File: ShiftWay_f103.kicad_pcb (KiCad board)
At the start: 2 copper layers, 120 parts, among them J1 GPIO, J2 3v3/GND, Q1 MMBTA42, Q2 MMBT5551L, Q3 STN93003, U1 STM32F103C8Tx, U2 XL7005A, U3 ICW6215, U4 LM1117DT-3.3, U5 MPU-6500

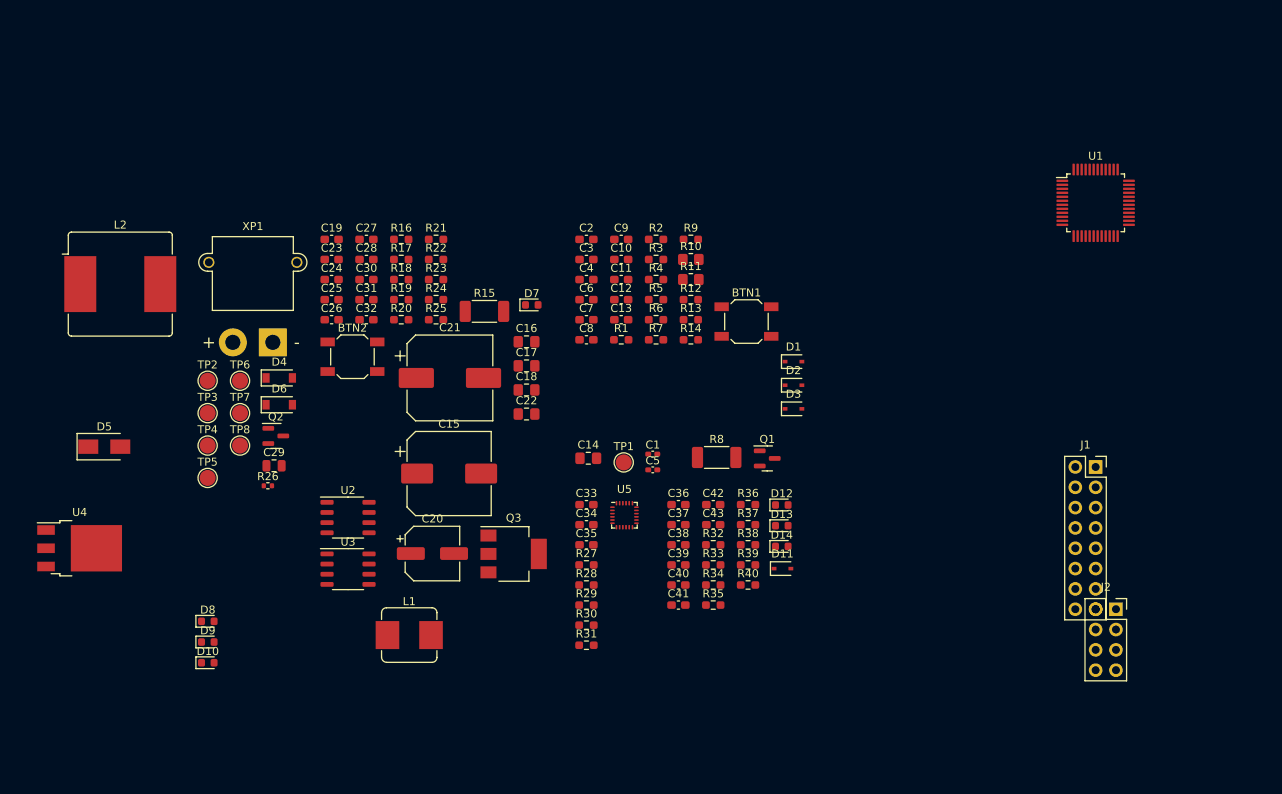
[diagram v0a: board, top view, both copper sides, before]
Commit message: Fixed short cirquit, minors
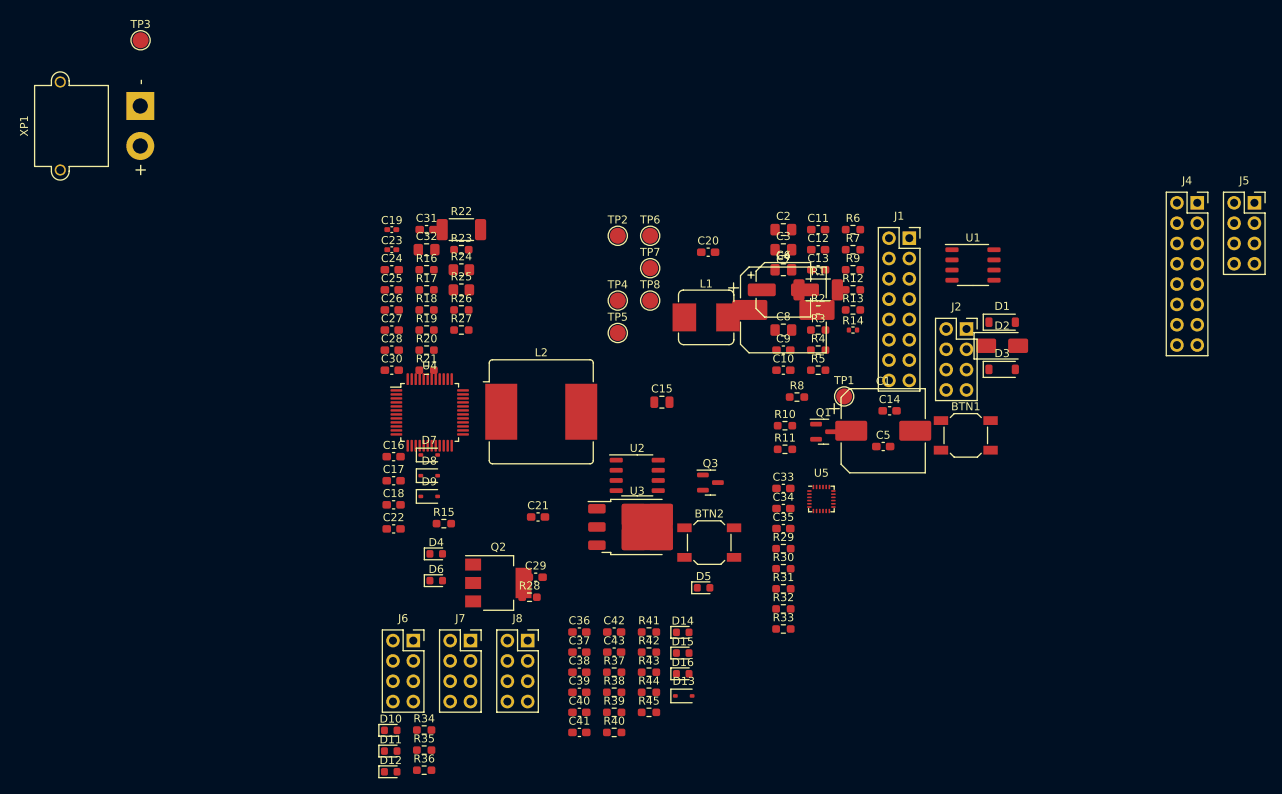
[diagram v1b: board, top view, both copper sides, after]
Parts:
- added D15: LED_G, LED_SMD:LED_0603_1608Metric, F.Cu at (118.6, 109.6)
- added D16: LED_G, LED_SMD:LED_0603_1608Metric, F.Cu at (118.6, 112.2)
- added J4: GPIO, Connector_PinSocket_2.54mm:PinSocket_2x08_P2.54mm_Vertical, F.Cu at (182.9, 53.3)
- added J5: GND/3V3, Connector_PinSocket_2.54mm:PinSocket_2x04_P2.54mm_Vertical, F.Cu at (190.0, 53.3)
- added J6: Conn_02x04, Connector_PinSocket_2.54mm:PinSocket_2x04_P2.54mm_Vertical, F.Cu at (84.9, 108.1)
- added J7: Conn_02x04, Connector_PinSocket_2.54mm:PinSocket_2x04_P2.54mm_Vertical, F.Cu at (92.0, 108.1)
- added J8: Conn_02x04, Connector_PinSocket_2.54mm:PinSocket_2x04_P2.54mm_Vertical, F.Cu at (99.2, 108.1)
- added R41: 4k3, Resistor_SMD:R_0603_1608Metric_Pad0.98x0.95mm_HandSolder, F.Cu at (114.3, 107.0)
- added R42: 4k3, Resistor_SMD:R_0603_1608Metric_Pad0.98x0.95mm_HandSolder, F.Cu at (114.3, 109.5)
- added R43: 680R, Resistor_SMD:R_0603_1608Metric_Pad0.98x0.95mm_HandSolder, F.Cu at (114.3, 112.0)
- added R44: 680R, Resistor_SMD:R_0603_1608Metric_Pad0.98x0.95mm_HandSolder, F.Cu at (114.3, 114.5)
- added R45: 680R, Resistor_SMD:R_0603_1608Metric_Pad0.98x0.95mm_HandSolder, F.Cu at (114.3, 117.0)
- C1: value 18pF -> 22uF 200v; footprint Capacitor_SMD:C_0402_1005Metric_Pad0.74x0.62mm_HandSolder -> Capacitor_SMD:CP_Elec_10x10
- C11, C39, C41: value 0.1uF -> 10uF
- C14, C16, C17, C22: footprint Capacitor_SMD:C_0805_2012Metric_Pad1.18x1.45mm_HandSolder -> Capacitor_SMD:C_0603_1608Metric_Pad1.08x0.95mm_HandSolder
- C15: value 22uF 200v -> 10uF; footprint Capacitor_SMD:CP_Elec_10x10 -> Capacitor_SMD:C_0805_2012Metric
- C18: value 2.2uF 50v -> 10uF; footprint Capacitor_SMD:C_0805_2012Metric_Pad1.18x1.45mm_HandSolder -> Capacitor_SMD:C_0603_1608Metric_Pad1.08x0.95mm_HandSolder
- C19: value 22nF -> 18pF; footprint Capacitor_SMD:C_0603_1608Metric_Pad1.08x0.95mm_HandSolder -> Capacitor_SMD:C_0402_1005Metric_Pad0.74x0.62mm_HandSolder
- C2, C3, C8: footprint Capacitor_SMD:C_0603_1608Metric_Pad1.08x0.95mm_HandSolder -> Capacitor_SMD:C_0805_2012Metric_Pad1.18x1.45mm_HandSolder
- C20: value 220uF 16v -> 0.1uF; footprint Capacitor_SMD:CP_Elec_6.3x7.7 -> Capacitor_SMD:C_0603_1608Metric_Pad1.08x0.95mm_HandSolder
- C21: value 470uF 25v -> 0.1uF; footprint Capacitor_SMD:CP_Elec_10x10.5 -> Capacitor_SMD:C_0603_1608Metric_Pad1.08x0.95mm_HandSolder
- C23: value 0.1uF -> 18pF; footprint Capacitor_SMD:C_0603_1608Metric_Pad1.08x0.95mm_HandSolder -> Capacitor_SMD:C_0402_1005Metric_Pad0.74x0.62mm_HandSolder
- C25, C40, C42: value 10uF -> 0.1uF
- C29: value 10uF -> 0.1uF; footprint Capacitor_SMD:C_0805_2012Metric -> Capacitor_SMD:C_0603_1608Metric_Pad1.08x0.95mm_HandSolder
- C32: value 10uF -> 0.1uF; footprint Capacitor_SMD:C_0603_1608Metric_Pad1.08x0.95mm_HandSolder -> Capacitor_SMD:C_0805_2012Metric_Pad1.18x1.45mm_HandSolder
- C4: value 0.1uF -> 2.2uF 50v; footprint Capacitor_SMD:C_0603_1608Metric_Pad1.08x0.95mm_HandSolder -> Capacitor_SMD:C_0805_2012Metric_Pad1.18x1.45mm_HandSolder
- C5: value 18pF -> 22nF; footprint Capacitor_SMD:C_0402_1005Metric_Pad0.74x0.62mm_HandSolder -> Capacitor_SMD:C_0603_1608Metric_Pad1.08x0.95mm_HandSolder
- C6: value 0.1uF -> 220uF 16v; footprint Capacitor_SMD:C_0603_1608Metric_Pad1.08x0.95mm_HandSolder -> Capacitor_SMD:CP_Elec_6.3x7.7
- C7: value 0.1uF -> 470uF 25v; footprint Capacitor_SMD:C_0603_1608Metric_Pad1.08x0.95mm_HandSolder -> Capacitor_SMD:CP_Elec_10x10.5
- D1, D3: value 1N4148WS -> MBR0530; footprint Diode_SMD:D_SOD-323 -> Diode_SMD:D_SOD-123
- D11: value 1N4148WS -> LED_R; footprint Diode_SMD:D_SOD-323 -> LED_SMD:LED_0603_1608Metric
- D12: value LED_G -> LED_R
- D13, D7: value LED_G -> 1N4148WS; footprint LED_SMD:LED_0603_1608Metric -> Diode_SMD:D_SOD-323
- D2: value 1N4148WS -> US1D; footprint Diode_SMD:D_SOD-323 -> Diode_SMD:D_SMA
- D4, D6: value MBR0530 -> LED_G; footprint Diode_SMD:D_SOD-123 -> LED_SMD:LED_0603_1608Metric
- D5: value US1D -> LED_G; footprint Diode_SMD:D_SMA -> LED_SMD:LED_0603_1608Metric
- D8, D9: value LED_R -> 1N4148WS; footprint LED_SMD:LED_0603_1608Metric -> Diode_SMD:D_SOD-323
- Q1: value MMBTA42 -> MMBT5551L
- Q2: value MMBT5551L -> STN93003; footprint Package_TO_SOT_SMD:SOT-23 -> Package_TO_SOT_SMD:SOT-223-3_TabPin2
- Q3: value STN93003 -> MMBTA42; footprint Package_TO_SOT_SMD:SOT-223-3_TabPin2 -> Package_TO_SOT_SMD:SOT-23
- R1: value 4k3 -> 100R 1W; footprint Resistor_SMD:R_0603_1608Metric_Pad0.98x0.95mm_HandSolder -> Resistor_SMD:R_2010_5025Metric_Pad1.40x2.65mm_HandSolder
- R10: value 81k 1% -> 2k2; footprint Resistor_SMD:R_0805_2012Metric_Pad1.20x1.40mm_HandSolder -> Resistor_SMD:R_0603_1608Metric_Pad0.98x0.95mm_HandSolder
- R11: value 2k2 1% -> 2k2; footprint Resistor_SMD:R_0805_2012Metric_Pad1.20x1.40mm_HandSolder -> Resistor_SMD:R_0603_1608Metric_Pad0.98x0.95mm_HandSolder
- R12: value 2k2 -> 1k
- R14: value 2k2 -> 680R; footprint Resistor_SMD:R_0603_1608Metric_Pad0.98x0.95mm_HandSolder -> Resistor_SMD:R_0402_1005Metric
- R15: value 100R 1W -> 4k3; footprint Resistor_SMD:R_2010_5025Metric_Pad1.40x2.65mm_HandSolder -> Resistor_SMD:R_0603_1608Metric_Pad0.98x0.95mm_HandSolder
- R19: value 6k8 -> 2k2
- R21, R23: value 81k -> 2k2
- R22: value 6k8 -> 1k 1W; footprint Resistor_SMD:R_0603_1608Metric_Pad0.98x0.95mm_HandSolder -> Resistor_SMD:R_2010_5025Metric_Pad1.40x2.65mm_HandSolder
- R24: value 2k2 -> 81k 1%; footprint Resistor_SMD:R_0603_1608Metric_Pad0.98x0.95mm_HandSolder -> Resistor_SMD:R_0805_2012Metric_Pad1.20x1.40mm_HandSolder
- R25: value 2k2 -> 2k2 1%; footprint Resistor_SMD:R_0603_1608Metric_Pad0.98x0.95mm_HandSolder -> Resistor_SMD:R_0805_2012Metric_Pad1.20x1.40mm_HandSolder
- R26: footprint Resistor_SMD:R_0402_1005Metric -> Resistor_SMD:R_0603_1608Metric_Pad0.98x0.95mm_HandSolder
- R27, R28: value 10k -> 2k2
- R32, R33: value 4k3 -> 10k
- R34, R35, R36: value 4k3 -> 1k
- R38, R39, R40: value 2k2 -> 4k3
- R5: value 2k2 -> 6k8
- R7, R9: value 2k2 -> 81k
- R8: value 1k 1W -> 6k8; footprint Resistor_SMD:R_2010_5025Metric_Pad1.40x2.65mm_HandSolder -> Resistor_SMD:R_0603_1608Metric_Pad0.98x0.95mm_HandSolder
- TP1: value SENBAT -> PWRON
- TP2: value PWRON -> PWRBUT
- TP3: value PWRBUT -> VBAT1
- TP4: value VBAT1 -> VBAT2
- TP5: value VBAT2 -> 5V
- TP6: value 5V -> 12V
- TP7: value 12V -> 3V3
- TP8: value 3V3 -> SENBAT
- U1: value STM32F103C8Tx -> XL7005A; footprint Package_QFP:LQFP-48_7x7mm_P0.5mm -> Package_SO:SOP-8_3.9x4.9mm_P1.27mm
- U2: value XL7005A -> ICW6215
- U3: value ICW6215 -> LM1117DT-3.3; footprint Package_SO:SOP-8_3.9x4.9mm_P1.27mm -> Package_TO_SOT_SMD:TO-252-3_TabPin2
- U4: value LM1117DT-3.3 -> STM32F103C8Tx; footprint Package_TO_SOT_SMD:TO-252-3_TabPin2 -> Package_QFP:LQFP-48_7x7mm_P0.5mm
- moved D5 77.0 mm to (121.2, 101.5)
- moved D12 59.2 mm to (82.1, 124.5)
- moved L2 55.0 mm to (100.9, 79.5)
- moved TP2 54.4 mm to (110.4, 57.5)
- moved TP4 54.4 mm to (110.4, 65.6)
- moved TP5 54.4 mm to (110.4, 69.6)
- moved TP6 54.4 mm to (114.5, 57.5)
- moved TP7 54.4 mm to (114.5, 61.5)
- moved TP8 54.4 mm to (114.5, 65.6)
- moved L1 54.4 mm to (121.5, 67.7)
- moved D11 54.0 mm to (82.1, 121.9)
- moved R36 52.3 mm to (86.2, 124.3)
- moved C20 51.1 mm to (121.7, 59.5)
- moved BTN2 50.3 mm to (121.9, 95.8)
- moved TP3 47.4 mm to (50.8, 33.0)
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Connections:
- net /Hall Sensors/HOLC_LED_K renamed Net-(D14-K)
- BTN1 pad 1: Net-(X2-Pin_2) -> Net-(J1-Pin_2)
- BTN1 pad 2: +3V3 -> Net-(J1-Pin_1)
- BTN2 pad 1: Net-(X6-Pin_1) -> Net-(X2-Pin_2)
- BTN2 pad 2: Net-(X6-Pin_2) -> +3V3
- C1 pad 1: OSCI -> +BATT
- C1 pad 2: +3V3 -> GND
- C10 pad 1: +3V3 -> +12V
- C10 pad 2: +3V3 -> GND
- C11 pad 1: +3V3 -> +5V
- C11 pad 2: +3V3 -> GND
- C12 pad 1: Net-(D1-K) -> +3V3
- C12 pad 2: +3V3 -> GND
- C13 pad 2: +3V3 -> GND
- C14 pad 1: +BATT -> +3V3
- C14 pad 2: +3V3 -> GND
- C15 pad 1: +BATT -> +3V3
- C15 pad 2: +3V3 -> GND
- C16 pad 1: Net-(Q3-E) -> +3V3
- C16 pad 2: +3V3 -> GND
- C17 pad 1: Net-(Q3-E) -> +5V
- C17 pad 2: +3V3 -> GND
- C18 pad 1: Net-(D6-K) -> +3V3
- C18 pad 2: Net-(D5-K) -> GND
- C19 pad 1: +5V -> OSCI
- C19 pad 2: +3V3 -> GND
- C2 pad 1: +3V3 -> VIN
- C2 pad 2: +3V3 -> GND
- C20 pad 1: +5V -> GND
- C21 pad 1: +12V -> GND
- C22 pad 1: +BATT -> +3V3
- C22 pad 2: +3V3 -> GND
- C23 pad 1: +3V3 -> OSCO
- C23 pad 2: +3V3 -> GND
- C24 pad 1: +12V -> +3V3
- C24 pad 2: +3V3 -> GND
- C25 pad 1: +5V -> +3V3
- C25 pad 2: +3V3 -> GND
- C26 pad 2: +3V3 -> GND
- C27 pad 2: +3V3 -> GND
- C28 pad 2: +3V3 -> GND
- C29 pad 2: +3V3 -> GND
- C3 pad 1: +3V3 -> VIN
- C3 pad 2: +3V3 -> GND
- C30 pad 1: +3V3 -> Net-(D7-K)
- C30 pad 2: +3V3 -> GND
- C31 pad 1: +5V -> +3V3
- C31 pad 2: +3V3 -> GND
- C32 pad 1: +3V3 -> +BATT
- C32 pad 2: +3V3 -> GND
- C33 pad 2: +3V3 -> GND
- C34 pad 2: +3V3 -> GND
- C35 pad 1: +3V3 -> GND
- C36 pad 2: +3V3 -> GND
- C37 pad 2: +3V3 -> GND
- C38 pad 2: +3V3 -> GND
- C39 pad 2: +3V3 -> GND
- C4 pad 1: +3V3 -> Net-(D3-K)
- C4 pad 2: +3V3 -> Net-(D2-K)
- C40 pad 2: +3V3 -> GND
- C41 pad 1: +3V3 -> Net-(D13-K)
- C41 pad 2: +3V3 -> GND
- C42 pad 1: HOL+5 -> Net-(D13-K)
- C42 pad 2: +3V3 -> GND
- C43 pad 1: HOL+5 -> +5V
- C43 pad 2: +3V3 -> GND
- C5 pad 1: OSCO -> +5V
- C5 pad 2: +3V3 -> GND
- C6 pad 1: +3V3 -> +5V
- C6 pad 2: +3V3 -> GND
- C7 pad 1: +3V3 -> +12V
- C7 pad 2: +3V3 -> GND
- C8 pad 1: +3V3 -> +BATT
- C8 pad 2: +3V3 -> GND
- C9 pad 2: +3V3 -> GND
- D1 pad 2: +3V3 -> GND
- D10 pad 1: +3V3 -> GND
- D10 pad 2: SDB -> Net-(D10-A)
- D11 pad 1: HOL+5 -> GND
- D11 pad 2: +5V -> Net-(D11-A)
- D12 pad 1: /Hall Sensors/HOLA_LED_K -> GND
- D13 pad 1: /Hall Sensors/HOLB_LED_K -> Net-(D13-K)
- D13 pad 2: Net-(D13-A) -> +5V
- D2 pad 2: Net-(D2-A) -> GND
- D3 pad 2: +3V3 -> +12V
- D4 pad 1: Net-(D4-K) -> GND
- D4 pad 2: +3V3 -> Net-(D4-A)
- D5 pad 1: Net-(D5-K) -> GND
- D5 pad 2: +3V3 -> Net-(D5-A)
- D6 pad 2: +12V -> +3V3
- D7 pad 1: /Power/PWR_LED_K -> Net-(D7-K)
- D8 pad 1: +3V3 -> Net-(D8-K)
- D8 pad 2: +3V3 -> Net-(D8-A)
- D9 pad 1: +3V3 -> Net-(D9-K)
- D9 pad 2: SDA -> GND
- L1 pad 1: Net-(D4-K) -> Net-(D1-K)
- L2 pad 1: Net-(D5-K) -> Net-(D2-K)
- Q1 pad 1: Net-(D3-K) -> Net-(Q1-B)
- Q1 pad 2: +3V3 -> GND
- Q1 pad 3: Net-(D2-A) -> Net-(Q1-C)
- Q2 pad 2: +3V3 -> +BATT
- Q2 pad 3: Net-(Q2-C) -> VIN
- Q3 pad 1: Net-(Q3-B) -> Net-(D9-K)
- Q3 pad 2: +BATT -> GND
- Q3 pad 3: Net-(Q3-E) -> Net-(D8-A)
- R1 pad 1: STATE -> +BATT
- R1 pad 2: +3V3 -> Net-(R1-Pad2)
- R10 pad 1: +BATT -> Net-(J1-Pin_1)
- R10 pad 2: Net-(R10-Pad2) -> GND
- R11 pad 1: Net-(R10-Pad2) -> Net-(J1-Pin_1)
- R11 pad 2: +3V3 -> POWERBUT
- R12 pad 1: Net-(X2-Pin_2) -> +5V
- R12 pad 2: MOTORBUT -> Net-(D4-A)
- R13 pad 1: Net-(R10-Pad2) -> +12V
- R13 pad 2: SENBAT -> Net-(D5-A)
- R14 pad 1: MOTORBUT -> GND
- R14 pad 2: +3V3 -> Net-(D6-K)
- R15 pad 1: +BATT -> STATE
- R15 pad 2: Net-(R15-Pad2) -> +3V3
- R16 pad 1: Net-(Q2-B) -> Net-(U4-NRST)
- R16 pad 2: POWERON -> GND
- R17 pad 1: Net-(Q2-B) -> MOSI
- R17 pad 2: +3V3 -> Net-(X1-Pin_2)
- R18 pad 1: Net-(Q3-E) -> MISO
- R18 pad 2: Net-(Q3-B) -> Net-(X1-Pin_3)
- R19 pad 1: +5V -> SCK
- R19 pad 2: +3V3 -> Net-(X1-Pin_4)
- R2 pad 1: Net-(U1-NRST) -> Net-(Q1-B)
- R2 pad 2: +3V3 -> POWERON
- R20 pad 1: +3V3 -> CS_MPU
- R20 pad 2: +3V3 -> Net-(X1-Pin_5)
- R21 pad 1: Net-(X6-Pin_1) -> BUZZER
- R21 pad 2: Net-(Q3-B) -> Net-(D9-K)
- R22 pad 1: Net-(X6-Pin_1) -> +BATT
- R22 pad 2: Net-(Q2-C) -> Net-(D8-K)
- R23 pad 1: Net-(X6-Pin_1) -> Net-(D9-K)
- R23 pad 2: Net-(Q3-B) -> GND
- R24 pad 1: Net-(X6-Pin_2) -> +BATT
- R24 pad 2: +3V3 -> Net-(R24-Pad2)
- R25 pad 1: Net-(X6-Pin_2) -> Net-(R24-Pad2)
- R25 pad 2: POWERBUT -> GND
- R26 pad 1: +3V3 -> Net-(X2-Pin_2)
- R26 pad 2: /Power/PWR_LED_K -> MOTORBUT
- R27 pad 1: MOSI -> Net-(R24-Pad2)
- R27 pad 2: +3V3 -> SENBAT
- R28 pad 1: +3V3 -> MOTORBUT
- R28 pad 2: MISO -> GND
- R29 pad 1: SCK -> MOSI
- R3 pad 1: MOSI -> Net-(Q1-B)
- R3 pad 2: Net-(X1-Pin_2) -> GND
- R30 pad 1: CS_MPU -> GND
- R30 pad 2: +3V3 -> MISO
- R31 pad 1: Net-(U5-FSYNC) -> SCK
- R32 pad 1: Net-(X9-Pin_2) -> CS_MPU
- R33 pad 1: Net-(X9-Pin_2) -> Net-(U5-FSYNC)
- R33 pad 2: HOLA -> GND
- R34 pad 1: Net-(X9-Pin_3) -> SDA
- R34 pad 2: +3V3 -> Net-(D10-A)
- R35 pad 1: Net-(X9-Pin_3) -> +3V3
- R35 pad 2: HOLB -> Net-(D11-A)
- R36 pad 1: Net-(X9-Pin_4) -> SDB
- R36 pad 2: +3V3 -> Net-(D12-A)
- R37 pad 1: Net-(X9-Pin_4) -> Net-(JH1-Pin_2)
- R37 pad 2: HOLC -> +3V3
- R38 pad 1: Net-(D12-A) -> Net-(JH1-Pin_2)
- R38 pad 2: +3V3 -> HOLA
- R39 pad 1: Net-(D13-A) -> Net-(JH1-Pin_3)
- R4 pad 1: MISO -> VIN
- R4 pad 2: Net-(X1-Pin_3) -> Net-(Q2-B)
- R40 pad 1: Net-(D14-A) -> Net-(JH1-Pin_3)
- R40 pad 2: +3V3 -> HOLB
- R5 pad 1: SCK -> +5V
- R5 pad 2: Net-(X1-Pin_4) -> GND
- R6 pad 1: CS_MPU -> GND
- R6 pad 2: Net-(X1-Pin_5) -> GND
- R7 pad 1: BUZZER -> Net-(J1-Pin_2)
- R7 pad 2: Net-(D3-K) -> Net-(Q2-B)
- R8 pad 1: +BATT -> Net-(J1-Pin_2)
- R8 pad 2: Net-(D2-K) -> Net-(Q1-C)
- R9 pad 1: Net-(D3-K) -> Net-(J1-Pin_2)
- R9 pad 2: +3V3 -> Net-(Q2-B)
- TP1 pad 1: SENBAT -> POWERON
- TP2 pad 1: POWERON -> POWERBUT
- TP3 pad 1: POWERBUT -> VIN
- TP4 pad 1: Net-(Q3-E) -> +BATT
- TP5 pad 1: +BATT -> +5V
- TP6 pad 1: +5V -> +12V
- TP7 pad 1: +12V -> +3V3
- TP8 pad 1: +3V3 -> SENBAT
- U1 pad 1: unconnected-(U1-VBAT-Pad1) -> +12V
- U1 pad 2: GPIO_PB13 -> Net-(D1-K)
- U1 pad 3: GPIO_PB14 -> GND
- U1 pad 4: GPIO_PB15 -> unconnected-(U1-EN-Pad4)
- U1 pad 5: OSCI -> GND
- U1 pad 6: OSCO -> GND
- U1 pad 7: Net-(U1-NRST) -> GND
- U1 pad 8: +3V3 -> GND
- U2 pad 1: +12V -> Net-(D3-K)
- U2 pad 2: Net-(D4-K) -> unconnected-(U2-NC-Pad2)
- U2 pad 3: +3V3 -> unconnected-(U2-FB-Pad3)
- U2 pad 5: +3V3 -> Net-(R1-Pad2)
- U2 pad 6: +3V3 -> Net-(R1-Pad2)
- U2 pad 7: +3V3 -> unconnected-(U2-NC-Pad7)
- U2 pad 8: +3V3 -> Net-(D2-K)
- U3 pad 1: Net-(D6-K) -> GND
- U3 pad 2: unconnected-(U3-NC-Pad2) -> +3V3
- U3 pad 3: unconnected-(U3-FB-Pad3) -> +5V
- U4 pad 1: +3V3 -> unconnected-(U4-VBAT-Pad1)
- U4 pad 2: +3V3 -> HOLC
- U4 pad 3: +5V -> HOLB
- U5 pad 18: +3V3 -> GND
- U5 pad 20: +3V3 -> GND
- XP1 pad 1: (no net) -> VIN
- XP1 pad 2: (no net) -> GND

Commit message: Fix mistakes
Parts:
- moved Q2 73.9 mm to (134.6, 38.1)
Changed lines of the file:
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@@
   )
   (footprint "Package_TO_SOT_SMD:SOT-223-3_TabPin2" (layer "F.Cu")
-    (at 95.5175 100.86)
+    (at 134.62 38.1)
     (descr "module CMS SOT223 4 pins")
     (tags "CMS SOT")

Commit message: topology in progress
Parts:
- removed XP1: POWER, Connector_AMASS:AMASS_XT30PW-M_1x02_P2.50mm_Horizontal
- added C44: 10uF, Capacitor_SMD:C_0603_1608Metric_Pad1.08x0.95mm_HandSolder, F.Cu at (125.8, 298.3)
- added C45: 10uF, Capacitor_SMD:C_0603_1608Metric_Pad1.08x0.95mm_HandSolder, F.Cu at (238.7, 314.1)
- added C46: 10uF, Capacitor_SMD:C_0603_1608Metric_Pad1.08x0.95mm_HandSolder, F.Cu at (15.6, 299.7)
- added C47: 10uF, Capacitor_SMD:C_0603_1608Metric_Pad1.08x0.95mm_HandSolder, F.Cu at (131.9, 299.8)
- added C48: 10uF, Capacitor_SMD:C_0603_1608Metric_Pad1.08x0.95mm_HandSolder, F.Cu at (266.5, 312.4)
- added C49: 10uF, Capacitor_SMD:C_0603_1608Metric_Pad1.08x0.95mm_HandSolder, F.Cu at (363.1, 3.69)
- added C50: 0.1uF, Capacitor_SMD:C_0603_1608Metric_Pad1.08x0.95mm_HandSolder, F.Cu at (363.1, 6.20)
- added C51: 10uF, Capacitor_SMD:C_0603_1608Metric_Pad1.08x0.95mm_HandSolder, F.Cu at (360.5, 10.2)
- added C52: 0.1uF, Capacitor_SMD:C_0603_1608Metric_Pad1.08x0.95mm_HandSolder, F.Cu at (360.5, 12.7)
- added C53: 0.1uF, Capacitor_SMD:C_0603_1608Metric_Pad1.08x0.95mm_HandSolder, F.Cu at (439.8, 34.0)
- added C54: 10nF, Capacitor_SMD:C_0603_1608Metric_Pad1.08x0.95mm_HandSolder, F.Cu at (380.1, 5.08)
- added C55: 10nF, Capacitor_SMD:C_0603_1608Metric_Pad1.08x0.95mm_HandSolder, F.Cu at (380.1, 3.11)
- added C56: 10nF, Capacitor_SMD:C_0603_1608Metric_Pad1.08x0.95mm_HandSolder, F.Cu at (350.9, 22.4)
- added C57: 0.1uF, Capacitor_SMD:C_0805_2012Metric_Pad1.18x1.45mm_HandSolder, F.Cu at (-108.7, -74.0)
- added D17: BZT52Bxx, Diode_SMD:D_SOD-123F, F.Cu at (249.9, 326.0)
- added D18: LED_R, LED_SMD:LED_0603_1608Metric, F.Cu at (41.4, 304.8)
- added D19: LED_R, LED_SMD:LED_0603_1608Metric, F.Cu at (111.8, 326.7)
- added D20: LED_R, LED_SMD:LED_0603_1608Metric, F.Cu at (241.2, 321.0)
- added D21: 1N4148WS, Diode_SMD:D_SOD-323, F.Cu at (382.6, 9.75)
- added D22: HALL_A, LED_SMD:LED_0603_1608Metric, F.Cu at (461.2, 37.6)
- added D23: HALL_B, LED_SMD:LED_0603_1608Metric, F.Cu at (461.2, 34.6)
- added D24: HALL_C, LED_SMD:LED_0603_1608Metric, F.Cu at (461.2, 31.7)
- added INTER1: Conn 2x4, Connector_PinHeader_2.54mm:PinHeader_2x04_P2.54mm_Vertical, F.Cu at (35.6, 327.7)
- added INTER2: Conn 2x4, Connector_PinHeader_2.54mm:PinHeader_2x04_P2.54mm_Vertical, F.Cu at (127.0, 330.2)
- added INTER3: Conn 2x4, Connector_PinHeader_2.54mm:PinHeader_2x04_P2.54mm_Vertical, F.Cu at (264.2, 327.7)
- added J10: GPIO, Connector_PinSocket_2.54mm:PinSocket_2x08_P2.54mm_Vertical, F.Cu at (-114.3, 50.8)
- added J11: JST_06, Connector_JST:JST_EH_B6B-EH-A_1x06_P2.50mm_Vertical, F.Cu at (-140.1, -69.2)
- added J12: Bluetooth, Connector_PinSocket_2.54mm:PinSocket_1x05_P2.54mm_Vertical, F.Cu at (-111.8, -82.9)
- added J13: GND/3V3, Connector_PinSocket_2.54mm:PinSocket_2x04_P2.54mm_Vertical, F.Cu at (-125.1, 37.2)
- added J3: 3V3 OUTLET, Connector_JST:JST_XH_B2B-XH-A_1x02_P2.50mm_Vertical, F.Cu at (424.2, -147.1)
- added J9: BuzzerLV, Connector_JST:JST_XH_B2B-XH-A_1x02_P2.50mm_Vertical, F.Cu at (-66.0, 11.6)
- added R46: 680R, Resistor_SMD:R_0603_1608Metric_Pad0.98x0.95mm_HandSolder, F.Cu at (451.2, 38.1)
- added R47: 680R, Resistor_SMD:R_0603_1608Metric_Pad0.98x0.95mm_HandSolder, F.Cu at (439.8, 36.5)
- added R48: 4k3, Resistor_SMD:R_0603_1608Metric_Pad0.98x0.95mm_HandSolder, F.Cu at (369.2, 10.2)
- added R49: 4k3, Resistor_SMD:R_0603_1608Metric_Pad0.98x0.95mm_HandSolder, F.Cu at (364.9, 10.2)
- added R50: 4k3, Resistor_SMD:R_0603_1608Metric_Pad0.98x0.95mm_HandSolder, F.Cu at (364.9, 12.7)
- added R51: 4k3, Resistor_SMD:R_0603_1608Metric_Pad0.98x0.95mm_HandSolder, F.Cu at (364.9, 15.2)
- added R52: 4k3, Resistor_SMD:R_0603_1608Metric_Pad0.98x0.95mm_HandSolder, F.Cu at (364.9, 17.7)
- added R53: 4k3, Resistor_SMD:R_0603_1608Metric_Pad0.98x0.95mm_HandSolder, F.Cu at (376.1, 22.2)
- added TP9: SENBAT, TestPoint:TestPoint_Pad_D2.0mm, F.Cu at (-86.5, -85.2)
- added U6: IR2184, Package_SO:SOIC-8-1EP_3.9x4.9mm_P1.27mm_EP2.514x3.2mm_ThermalVias, F.Cu at (35.7, 292.7)
- added U7: IR2184, Package_SO:SOIC-8-1EP_3.9x4.9mm_P1.27mm_EP2.514x3.2mm_ThermalVias, F.Cu at (127.0, 315.0)
- added U8: IR2184, Package_SO:SOIC-8-1EP_3.9x4.9mm_P1.27mm_EP2.514x3.2mm_ThermalVias, F.Cu at (256.4, 313.1)
- added XH1: Hall Sensors, Connector_Molex:Molex_Micro-Fit_3.0_43045-0600_2x03_P3.00mm_Horizontal, F.Cu at (360.2, 32.3)
- added XH2: Hall Tester, Connector_Molex:Molex_Micro-Fit_3.0_43045-0600_2x03_P3.00mm_Horizontal, F.Cu at (446.6, 29.7)
- added XT1: POWER, Connector_AMASS:AMASS_XT30PW-M_1x02_P2.50mm_Horizontal, F.Cu at (105.9, -79.0)
- added XTAL1: NX3225GD-8MHZ-STD-CRA-3, digikey-footprints:SMD-2_3.2x2.5mm, F.Cu at (-91.8, -72.6)
- C1: value 22uF 200v -> 820pF; footprint Capacitor_SMD:CP_Elec_10x10 -> Capacitor_SMD:C_0603_1608Metric_Pad1.08x0.95mm_HandSolder
- C10: value 0.1uF -> 22uF; footprint Capacitor_SMD:C_0603_1608Metric_Pad1.08x0.95mm_HandSolder -> Capacitor_SMD:CP_Elec_10x10
- C11: value 10uF -> 22uF; footprint Capacitor_SMD:C_0603_1608Metric_Pad1.08x0.95mm_HandSolder -> Capacitor_SMD:CP_Elec_10x10
- C12: value 0.1uF -> 1uF; footprint Capacitor_SMD:C_0603_1608Metric_Pad1.08x0.95mm_HandSolder -> Capacitor_SMD:CP_Elec_10x10
- C13, C14, C24, C25, C43, C9: value 0.1uF -> 10uF
- C15: value 10uF -> 150uF; footprint Capacitor_SMD:C_0805_2012Metric -> Capacitor_SMD:CP_Elec_10x10
- C18, C41: value 10uF -> 0.1uF
- C19: value 18pF -> 0.1uF; footprint Capacitor_SMD:C_0402_1005Metric_Pad0.74x0.62mm_HandSolder -> Capacitor_SMD:C_0805_2012Metric_Pad1.18x1.45mm_HandSolder
- C2: value 0.1uF -> 22nF; footprint Capacitor_SMD:C_0805_2012Metric_Pad1.18x1.45mm_HandSolder -> Capacitor_SMD:C_0603_1608Metric_Pad1.08x0.95mm_HandSolder
- C23: value 18pF -> 10uF; footprint Capacitor_SMD:C_0402_1005Metric_Pad0.74x0.62mm_HandSolder -> Capacitor_SMD:C_0603_1608Metric_Pad1.08x0.95mm_HandSolder
- C28, C29: value 0.1uF -> 18pF; footprint Capacitor_SMD:C_0603_1608Metric_Pad1.08x0.95mm_HandSolder -> Capacitor_SMD:C_0402_1005Metric_Pad0.74x0.62mm_HandSolder
- C3: value 0.1uF -> 220uF 16v; footprint Capacitor_SMD:C_0805_2012Metric_Pad1.18x1.45mm_HandSolder -> Capacitor_SMD:CP_Elec_6.3x7.7
- C32: footprint Capacitor_SMD:C_0805_2012Metric_Pad1.18x1.45mm_HandSolder -> Capacitor_SMD:C_0603_1608Metric_Pad1.08x0.95mm_HandSolder
- C33: value 0.01uF -> 0.1uF
- C36: value 10nF -> 0.1uF; footprint Capacitor_SMD:C_0603_1608Metric_Pad1.08x0.95mm_HandSolder -> Capacitor_SMD:C_0805_2012Metric_Pad1.18x1.45mm_HandSolder
- C37, C38: value 10nF -> 0.1uF
- C39: value 10uF -> 1uF
- C4: value 2.2uF 50v -> 51nF; footprint Capacitor_SMD:C_0805_2012Metric_Pad1.18x1.45mm_HandSolder -> Capacitor_SMD:C_0603_1608Metric_Pad1.08x0.95mm_HandSolder
- C40: value 0.1uF -> 0.01uF
- C5: value 22nF -> 0.1uF
- C6: value 220uF 16v -> 10uF; footprint Capacitor_SMD:CP_Elec_6.3x7.7 -> Capacitor_SMD:C_0603_1608Metric_Pad1.08x0.95mm_HandSolder
- C7: value 470uF 25v -> 10uF; footprint Capacitor_SMD:CP_Elec_10x10.5 -> Capacitor_SMD:C_0603_1608Metric_Pad1.08x0.95mm_HandSolder
- C8: value 0.1uF -> 10uF; footprint Capacitor_SMD:C_0805_2012Metric_Pad1.18x1.45mm_HandSolder -> Capacitor_SMD:C_0603_1608Metric_Pad1.08x0.95mm_HandSolder
- D10, D11, D12: value LED_R -> 1N4148WS; footprint LED_SMD:LED_0603_1608Metric -> Diode_SMD:D_SOD-323
- D14: value LED_G -> 1N4148WS; footprint LED_SMD:LED_0603_1608Metric -> Diode_SMD:D_SOD-323
- D15, D16: value LED_G -> BZT52Bxx; footprint LED_SMD:LED_0603_1608Metric -> Diode_SMD:D_SOD-123F
- D2: value US1D -> LED_G; footprint Diode_SMD:D_SMA -> LED_SMD:LED_0603_1608Metric
- D3: value MBR0530 -> 1N4148WS; footprint Diode_SMD:D_SOD-123 -> Diode_SMD:D_SOD-323
- D4, D6: value LED_G -> STTH1L06A; footprint LED_SMD:LED_0603_1608Metric -> Diode_SMD:D_SMA_Handsoldering
- D7: value 1N4148WS -> LED_G; footprint Diode_SMD:D_SOD-323 -> LED_SMD:LED_0603_1608Metric
- J1: value GPIO -> 12V OUTLET; footprint Connector_PinSocket_2.54mm:PinSocket_2x08_P2.54mm_Vertical -> Connector_JST:JST_XH_B2B-XH-A_1x02_P2.50mm_Vertical
- J2: value 3v3/GND -> 5V OUTLET; footprint Connector_PinSocket_2.54mm:PinSocket_2x04_P2.54mm_Vertical -> Connector_JST:JST_XH_B2B-XH-A_1x02_P2.50mm_Vertical
- J4: value GPIO -> PWRBTN; footprint Connector_PinSocket_2.54mm:PinSocket_2x08_P2.54mm_Vertical -> Connector_JST:JST_XH_B2B-XH-A_1x02_P2.50mm_Vertical
- J5: value GND/3V3 -> PWRONOUT; footprint Connector_PinSocket_2.54mm:PinSocket_2x04_P2.54mm_Vertical -> Connector_JST:JST_XH_B2B-XH-A_1x02_P2.50mm_Vertical
- J6: value Conn_02x04 -> MTRBTN; footprint Connector_PinSocket_2.54mm:PinSocket_2x04_P2.54mm_Vertical -> Connector_JST:JST_XH_B2B-XH-A_1x02_P2.50mm_Vertical
- J7: value Conn_02x04 -> SPI_DBG; footprint Connector_PinSocket_2.54mm:PinSocket_2x04_P2.54mm_Vertical -> Connector_PinSocket_2.54mm:PinSocket_1x06_P2.54mm_Vertical
- J8: value Conn_02x04 -> BuzzerHV; footprint Connector_PinSocket_2.54mm:PinSocket_2x04_P2.54mm_Vertical -> Connector_JST:JST_XH_B2B-XH-A_1x02_P2.50mm_Vertical
- L2: value 331uH -> 330uH
- Q1: value MMBT5551L -> BSS138; footprint Package_TO_SOT_SMD:SOT-23 -> digikey-footprints:SOT-23-3
- Q2: value STN93003 -> BSS138; footprint Package_TO_SOT_SMD:SOT-223-3_TabPin2 -> digikey-footprints:SOT-23-3
- R1: value 100R 1W -> 6k8; footprint Resistor_SMD:R_2010_5025Metric_Pad1.40x2.65mm_HandSolder -> Resistor_SMD:R_0603_1608Metric_Pad0.98x0.95mm_HandSolder
- R11: value 2k2 -> 210k; footprint Resistor_SMD:R_0603_1608Metric_Pad0.98x0.95mm_HandSolder -> Resistor_SMD:R_0805_2012Metric_Pad1.20x1.40mm_HandSolder
- R12: value 1k -> 5k6; footprint Resistor_SMD:R_0603_1608Metric_Pad0.98x0.95mm_HandSolder -> Resistor_SMD:R_0805_2012Metric_Pad1.20x1.40mm_HandSolder
- R14: value 680R -> 10k; footprint Resistor_SMD:R_0402_1005Metric -> Resistor_SMD:R_0603_1608Metric_Pad0.98x0.95mm_HandSolder
- R15, R39, R40, R41: value 4k3 -> 2k2
- R18: value 2k2 -> 81k 1%; footprint Resistor_SMD:R_0603_1608Metric_Pad0.98x0.95mm_HandSolder -> Resistor_SMD:R_0805_2012Metric_Pad1.20x1.40mm_HandSolder
- R2: value 2k2 -> 1k
- R21: value 2k2 -> 2k2 1%; footprint Resistor_SMD:R_0603_1608Metric_Pad0.98x0.95mm_HandSolder -> Resistor_SMD:R_0805_2012Metric_Pad1.20x1.40mm_HandSolder
- R22: value 1k 1W -> 2k2; footprint Resistor_SMD:R_2010_5025Metric_Pad1.40x2.65mm_HandSolder -> Resistor_SMD:R_0603_1608Metric_Pad0.98x0.95mm_HandSolder
- R23: value 2k2 -> 4k7
- R24: value 81k 1% -> 2k2; footprint Resistor_SMD:R_0805_2012Metric_Pad1.20x1.40mm_HandSolder -> Resistor_SMD:R_0603_1608Metric_Pad0.98x0.95mm_HandSolder
- R25: value 2k2 1% -> 1k5 1W; footprint Resistor_SMD:R_0805_2012Metric_Pad1.20x1.40mm_HandSolder -> Resistor_SMD:R_2010_5025Metric_Pad1.40x2.65mm_HandSolder
- R28: value 2k2 -> 10k
- R3: value 2k2 -> 100k
- R33: value 10k -> 2k2
- R34, R35: value 1k -> 2k2
- R36: value 1k -> 100
- R37, R38: value 4k3 -> 100
- R42: value 4k3 -> 1k
- R43, R44: value 680R -> 1k
- R5: value 6k8 -> 9k1
- R6: value 2k2 -> 100R 1W; footprint Resistor_SMD:R_0603_1608Metric_Pad0.98x0.95mm_HandSolder -> Resistor_SMD:R_2010_5025Metric_Pad1.40x2.65mm_HandSolder
- R7: value 81k -> 82k
- R8: value 6k8 -> 680R
- R9: value 81k -> 12k
- TP1: value PWRON -> VBAT1
- TP2: value PWRBUT -> 3V3
- TP3: value VBAT1 -> 12V
- TP4: value VBAT2 -> 5V
- TP5: value 5V -> 3V3
- TP6: value 12V -> 3VS
- TP7: value 3V3 -> PWRON
- TP8: value SENBAT -> PWRBUT
- U2: value ICW6215 -> VIPER115LS; footprint Package_SO:SOP-8_3.9x4.9mm_P1.27mm -> 4shift:SOIC100P600X175-10N
- U3: value LM1117DT-3.3 -> LM1117-3.3; footprint Package_TO_SOT_SMD:TO-252-3_TabPin2 -> Package_TO_SOT_SMD:SOT-223
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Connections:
- BTN1 pad 1: Net-(J1-Pin_2) -> 3VS
- BTN1 pad 2: Net-(J1-Pin_1) -> POWERBUT
- BTN2 pad 1: Net-(X2-Pin_2) -> Net-(J6-Pin_2)
- C1 pad 1: +BATT -> Net-(U2-COMP)
- C1 pad 2: GND -> VIPER_G
- C10 pad 1: +12V -> VIN
- C11 pad 1: +5V -> VIN
- C12 pad 1: +3V3 -> Net-(D3-K)
- C12 pad 2: GND -> VIPER_G
- C13 pad 1: +3V3 -> +5V
- C15 pad 1: +3V3 -> +12V
- C16 pad 1: +3V3 -> +12V
- C19 pad 1: OSCI -> VIN
- C2 pad 1: VIN -> +5V
- C2 pad 2: GND -> Net-(U1-FB)
- C20 pad 1: GND -> +3V3
- C20 pad 2: +3V3 -> GND
- C21 pad 1: GND -> +3V3
- C21 pad 2: +3V3 -> GND
- C23 pad 1: OSCO -> +3V3
- C26 pad 1: +3V3 -> Net-(D9-K)
- C28 pad 1: +3V3 -> OSCI
- C29 pad 1: +3V3 -> OSCO
- C3 pad 1: VIN -> +5V
- C30 pad 1: Net-(D7-K) -> +3V3
- C32 pad 1: +BATT -> +3V3
- C35 pad 1: GND -> +3V3
- C35 pad 2: Net-(U5-REGOUT) -> GND
- C36 pad 1: HOLA -> VIN
- C37 pad 1: HOLB -> +3V3
- C38 pad 1: HOLC -> GND
- C38 pad 2: GND -> +3V3
- C39 pad 1: +3V3 -> GND
- C39 pad 2: GND -> +3V3
- C4 pad 1: Net-(D3-K) -> Net-(C4-Pad1)
- C4 pad 2: Net-(D2-K) -> VIPER_G
- C41 pad 1: Net-(D13-K) -> +3V3
- C42 pad 1: Net-(D13-K) -> GND
- C42 pad 2: GND -> Net-(U5-REGOUT)
- C43 pad 1: +5V -> GND
- C43 pad 2: GND -> +12V
- C5 pad 1: +5V -> Net-(D3-A)
- C5 pad 2: GND -> VIPER_G
- C6 pad 1: +5V -> VIN
- C7 pad 1: +12V -> VIN
- C8 pad 1: +BATT -> VIN
- C9 pad 1: +3V3 -> VIN
- D10 pad 1: GND -> Net-(D10-K)
- D11 pad 1: GND -> Net-(D11-K)
- D11 pad 2: Net-(D11-A) -> GND
- D12 pad 1: GND -> Net-(D12-K)
- D12 pad 2: Net-(D12-A) -> +12V
- D13 pad 2: +5V -> +12V
- D14 pad 2: Net-(D14-A) -> +12V
- D15 pad 1: Net-(D15-K) -> Net-(D12-K)
- D16 pad 1: Net-(D16-K) -> Net-(D13-K)
- D2 pad 1: Net-(D2-K) -> GND
- D2 pad 2: GND -> Net-(D2-A)
- D3 pad 2: +12V -> Net-(D3-A)
- D4 pad 1: GND -> Net-(D3-A)
- D4 pad 2: Net-(D4-A) -> +12V
- D5 pad 1: GND -> Net-(D5-K)
- D5 pad 2: Net-(D5-A) -> +3V3
- D6 pad 1: Net-(D6-K) -> VIPER_G
- D6 pad 2: +3V3 -> GND
- D7 pad 1: Net-(D7-K) -> GND
- D7 pad 2: +3V3 -> Net-(D7-A)
- D8 pad 2: Net-(D8-A) -> GND
- D9 pad 2: GND -> +3V3
- J1 pad 1: GPIO_PB3 -> +12V
- J1 pad 2: GPIO_PB4 -> GND
- J2 pad 1: +3V3 -> +5V
- J2 pad 2: +3V3 -> GND
- J4 pad 1: GPIO_PB3 -> POWERBUT
- J4 pad 2: GPIO_PB4 -> 3VS
- J5 pad 2: GND -> Net-(D8-K)
- J6 pad 1: CUR1 -> +3V3
- J6 pad 2: +3V3 -> Net-(J6-Pin_2)
- J7 pad 1: SDC -> Net-(D9-K)
- J7 pad 2: DRC -> Net-(J7-Pin_2)
- J7 pad 3: +3V3 -> Net-(J7-Pin_3)
- J7 pad 4: +3V3 -> Net-(J7-Pin_4)
- J7 pad 5: +3V3 -> Net-(J7-Pin_5)
- J7 pad 6: +12V -> GND
- J8 pad 1: +3V3 -> Net-(D10-K)
- J8 pad 2: +12V -> Net-(D10-A)
- L2 pad 1: Net-(D2-K) -> VIPER_G
- Q1 pad 1: Net-(Q1-B) -> POWERBUT
- Q1 pad 3: Net-(Q1-C) -> DIS
- Q2 pad 1: Net-(Q2-B) -> Net-(D8-K)
- Q2 pad 2: +BATT -> GND
- Q2 pad 3: VIN -> DIS
- Q3 pad 1: Net-(D9-K) -> Net-(D11-K)
- Q3 pad 3: Net-(D8-A) -> Net-(D10-A)
- R1 pad 1: +BATT -> +5V
- R1 pad 2: Net-(R1-Pad2) -> Net-(U1-FB)
- R10 pad 1: Net-(J1-Pin_1) -> +12V
- R10 pad 2: GND -> Net-(D7-A)
- R11 pad 1: Net-(J1-Pin_1) -> VIN
- R11 pad 2: POWERBUT -> 3VS
- R12 pad 1: +5V -> 3VS
- R12 pad 2: Net-(D4-A) -> GND
- R13 pad 1: +12V -> Net-(D8-K)
- R13 pad 2: Net-(D5-A) -> POWERON
- R14 pad 1: GND -> DIS
- R14 pad 2: Net-(D6-K) -> 3VS
- R15 pad 1: STATE -> Net-(J6-Pin_2)
- R15 pad 2: +3V3 -> MOTORBUT
- R16 pad 1: Net-(U4-NRST) -> MOSI
- R16 pad 2: GND -> Net-(J7-Pin_2)
- R17 pad 1: MOSI -> MISO
- R17 pad 2: Net-(X1-Pin_2) -> Net-(J7-Pin_3)
- R18 pad 1: MISO -> VIN
- R18 pad 2: Net-(X1-Pin_3) -> Net-(R18-Pad2)
- R19 pad 1: SCK -> Net-(R18-Pad2)
- R19 pad 2: Net-(X1-Pin_4) -> SENBAT
- R2 pad 1: Net-(Q1-B) -> +5V
- R2 pad 2: POWERON -> Net-(D2-A)
- R20 pad 1: CS_MPU -> SCK
- R20 pad 2: Net-(X1-Pin_5) -> Net-(J7-Pin_4)
- R21 pad 1: BUZZER -> Net-(R18-Pad2)
- R21 pad 2: Net-(D9-K) -> GND
- R22 pad 1: +BATT -> CS_MPU
- R22 pad 2: Net-(D8-K) -> Net-(J7-Pin_5)
- R23 pad 1: Net-(D9-K) -> STATE
- R23 pad 2: GND -> +3V3
- R24 pad 1: +BATT -> Net-(U4-NRST)
- R24 pad 2: Net-(R24-Pad2) -> GND
- R25 pad 1: Net-(R24-Pad2) -> VIN
- R25 pad 2: GND -> Net-(D10-K)
- R26 pad 1: Net-(X2-Pin_2) -> BUZZER
- R26 pad 2: MOTORBUT -> Net-(D11-K)
- R27 pad 1: Net-(R24-Pad2) -> Net-(D11-K)
- R27 pad 2: SENBAT -> GND
- R28 pad 1: MOTORBUT -> MOSI
- R28 pad 2: GND -> +3V3
- R29 pad 1: MOSI -> SCK
- R3 pad 1: Net-(Q1-B) -> Net-(U2-COMP)
- R3 pad 2: GND -> Net-(C4-Pad1)
- R30 pad 1: GND -> CS_MPU
- R30 pad 2: MISO -> +3V3
- R31 pad 1: SCK -> GND
- R31 pad 2: +3V3 -> MISO
- R32 pad 1: CS_MPU -> Net-(U5-FSYNC)
- R32 pad 2: +3V3 -> GND
- R33 pad 1: Net-(U5-FSYNC) -> DRA
- R33 pad 2: GND -> Net-(U6-IN)
- R34 pad 1: SDA -> DRB
- R34 pad 2: Net-(D10-A) -> Net-(U7-IN)
- R35 pad 1: +3V3 -> DRC
- R35 pad 2: Net-(D11-A) -> Net-(U8-IN)
- R36 pad 1: SDB -> Net-(D15-A)
- R36 pad 2: Net-(D12-A) -> AK
- R37 pad 1: Net-(JH1-Pin_2) -> Net-(D16-A)
- R37 pad 2: +3V3 -> BK
- R38 pad 1: Net-(JH1-Pin_2) -> Net-(D17-A)
- R38 pad 2: HOLA -> CK
- R39 pad 1: Net-(JH1-Pin_3) -> Net-(U6-~{SD})
- R39 pad 2: +3V3 -> SDA
- R4 pad 1: VIN -> Net-(U1-FB)
- R4 pad 2: Net-(Q2-B) -> GND
- R40 pad 1: Net-(JH1-Pin_3) -> Net-(U7-~{SD})
- R40 pad 2: HOLB -> SDB
- R41 pad 1: Net-(JH1-Pin_4) -> Net-(U8-~{SD})
- R41 pad 2: +3V3 -> SDC
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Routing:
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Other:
- board text added: "BUZZR HV"
- board text added: "BUZZR LV"
- board text added: "MTR STOP"
- board text added: "PWR BTN"
- board text added: "PWR LV"

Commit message: Replaced unused GPIO, added SWD connectorm, PCB in progress
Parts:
- removed C38: 0.1uF, Capacitor_SMD:C_0603_1608Metric_Pad1.08x0.95mm_HandSolder
- removed C39: 1uF, Capacitor_SMD:C_0603_1608Metric_Pad1.08x0.95mm_HandSolder
- removed C6, C7, C8, C9: 10uF, Capacitor_SMD:C_0603_1608Metric_Pad1.08x0.95mm_HandSolder
- removed D8: 1N4148WS, Diode_SMD:D_SOD-323
- removed J13: GND/3V3, Connector_PinSocket_2.54mm:PinSocket_2x04_P2.54mm_Vertical
- added R54: 100, Resistor_SMD:R_0603_1608Metric_Pad0.98x0.95mm_HandSolder, F.Cu at (89.2, -130.6)
- added U9: LTV-817S, Package_DIP:SMDIP-4_W9.53mm, F.Cu at (85.1, -127.8)
- J10: value GPIO -> MCU_SWD; footprint Connector_PinSocket_2.54mm:PinSocket_2x08_P2.54mm_Vertical -> Connector_PinSocket_2.54mm:PinSocket_1x04_P2.54mm_Vertical
- moved D22 531.0 mm to (-33.8, -154.6)
- moved D23 531.0 mm to (-33.8, -157.5)
- moved D24 531.0 mm to (-33.8, -160.5)
- moved C53 531.0 mm to (-55.3, -158.2)
- moved R45 531.0 mm to (-43.8, -151.5)
- moved R46 531.0 mm to (-43.8, -154.0)
- moved R47 531.0 mm to (-55.3, -155.7)
- moved XH2 531.0 mm to (-48.5, -162.4)
- moved C49 497.0 mm to (-96.8, -184.8)
- moved C50 497.0 mm to (-96.8, -182.3)
- moved C56 497.0 mm to (-108.9, -166.0)
- moved D21 497.0 mm to (-77.3, -178.7)
- moved R49 497.0 mm to (-95.0, -178.3)
- moved R50 497.0 mm to (-95.0, -175.8)
- moved R51 497.0 mm to (-95.0, -173.3)
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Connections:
- net CUR2 renamed THB
- INTER1 pad 1: CUR1 -> GND
- INTER1 pad 4: AK -> CURA
- INTER1 pad 5: GND -> THA
- INTER1 pad 6: GND -> HOA
- INTER1 pad 7: LOA -> AK
- INTER1 pad 8: HOA -> LOA
- INTER2 pad 2: GND -> +3V3
- INTER2 pad 3: LOB -> GND
- INTER2 pad 4: HOB -> CURB
- INTER2 pad 6: BK -> HOB
- INTER2 pad 7: GND -> BK
- INTER2 pad 8: +3V3 -> LOB
- INTER3 pad 1: LOC -> GND
- INTER3 pad 2: HOC -> +3V3
- INTER3 pad 4: GND -> CURC
- INTER3 pad 5: +3V3 -> THC
- INTER3 pad 6: CK -> HOC
- INTER3 pad 7: CUR3 -> CK
- INTER3 pad 8: GND -> LOC
- J10 pad 1: GPIO_PB3 -> GND
- J10 pad 2: GPIO_PB4 -> MCU_SWCLK
- J10 pad 3: GPIO_PB5 -> MCU_SWDIO
- J10 pad 4: GPIO_PB9 -> +3V3
- J5 pad 1: GND -> Net-(J5-Pin_1)
- J5 pad 2: Net-(D8-K) -> Net-(J5-Pin_2)
- Q2 pad 1: Net-(D8-K) -> Net-(Q2-G)
- R13 pad 1: Net-(D8-K) -> Net-(Q2-G)
- TP7 pad 1: Net-(D8-K) -> Net-(Q2-G)
- U4 pad 10: GPIO_PA0 -> unconnected-(U4-PA0-Pad10)
- U4 pad 11: GPIO_PA1 -> unconnected-(U4-PA1-Pad11)
- U4 pad 12: CUR3 -> CURC
- U4 pad 13: CUR1 -> CURA
- U4 pad 14: GPIO_PA4 -> unconnected-(U4-PA4-Pad14)
- U4 pad 26: GPIO_PB13 -> MCU_SWCLK
- U4 pad 27: GPIO_PB14 -> MCU_SWDIO
- U4 pad 28: GPIO_PB15 -> unconnected-(U4-PB15-Pad28)
- U4 pad 32: GPIO_PA11 -> unconnected-(U4-PA11-Pad32)
- U4 pad 38: GPIO_PA15 -> unconnected-(U4-PA15-Pad38)
- U4 pad 39: GPIO_PB3 -> unconnected-(U4-PB3-Pad39)
- U4 pad 40: GPIO_PB4 -> unconnected-(U4-PB4-Pad40)
- U4 pad 41: GPIO_PB5 -> unconnected-(U4-PB5-Pad41)
- U4 pad 42: GPIO_PB9 -> unconnected-(U4-PB6-Pad42)
- U4 pad 45: GPIO_PB11 -> unconnected-(U4-PB8-Pad45)
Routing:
- net +12V: track 41.5 -> 104.4 mm, vias 0 -> 6
- net DIS: track 49.1 -> 7.87 mm, vias 2 -> 0
- net +5V: track 0.00 -> 32.7 mm
- net AK: track 0.00 -> 19.2 mm, vias 0 -> 1
- net BK: track 0.00 -> 18.4 mm, vias 0 -> 1
- net CK: track 0.00 -> 18.4 mm, vias 0 -> 1
- net MCU_SWDIO: track 0.00 -> 17.9 mm
- net MCU_SWCLK: track 0.00 -> 16.2 mm
- net HOA: track 0.00 -> 15.0 mm
- net Net-(D3-K): track 16.7 -> 31.1 mm
- net HOC: track 0.00 -> 14.4 mm
- net Net-(D8-K): track 14.4 -> 0.00 mm
- net HOB: track 0.00 -> 14.3 mm
- net Net-(J5-Pin_1): track 0.00 -> 13.5 mm
- net VIN: track 80.5 -> 67.2 mm
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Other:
- board text added: "12V"
- board text added: "3V3"
- board text added: "5V"
- board text added: "PWR OPTO"
- board text removed: "PWR LV"

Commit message: Fixes, layouting
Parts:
- removed C49, C51: 10uF, Capacitor_SMD:C_0603_1608Metric_Pad1.08x0.95mm_HandSolder
- removed TP2: 3V3, TestPoint:TestPoint_Pad_D2.0mm
- removed XT1: POWER, Connector_AMASS:AMASS_XT30PW-M_1x02_P2.50mm_Horizontal
- C23, C24, C25: value 10uF -> 0.1uF
- C57: footprint Capacitor_SMD:C_0805_2012Metric_Pad1.18x1.45mm_HandSolder -> Capacitor_SMD:C_0603_1608Metric_Pad1.08x0.95mm_HandSolder
- J7: footprint Connector_PinSocket_2.54mm:PinSocket_1x06_P2.54mm_Vertical -> Connector_PinSocket_1.27mm:PinSocket_1x07_P1.27mm_Vertical
- U9: value LTV-817S -> TLP291; footprint Package_DIP:SMDIP-4_W9.53mm -> Package_SO:SOIC-4_4.55x2.6mm_P1.27mm
- moved C56 380.3 mm to (190.6, 68.2), turned to -90 degrees
- moved C52 376.7 mm to (197.2, 56.4), turned to 90 degrees
- moved R50 375.5 mm to (193.9, 64.1), turned to 90 degrees
- moved C50 375.5 mm to (192.4, 57.2), turned to 180 degrees
- moved R52 374.9 mm to (193.9, 68.2), turned to 90 degrees
- moved R49 373.3 mm to (192.3, 60.0), turned to 90 degrees
- moved R51 372.7 mm to (192.3, 64.1), turned to 90 degrees
- moved R48 371.2 mm to (193.9, 60.0), turned to 90 degrees
- moved XH1 370.2 mm to (200.0, 61.1), turned to -90 degrees
- moved C55 367.8 mm to (190.6, 64.1), turned to -90 degrees
- moved C54 363.8 mm to (190.6, 60.0), turned to -90 degrees
- moved R53 362.2 mm to (192.3, 68.2), turned to 90 degrees
- moved D21 360.1 mm to (195.5, 56.4), turned to 90 degrees
- moved J11 348.6 mm to (207.1, 92.4), turned to -90 degrees
- moved XH2 344.6 mm to (200.0, 76.3), turned to -90 degrees
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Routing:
- net +3V3: track 58.1 -> 173.3 mm, vias 0 -> 7
- net +12V: track 104.4 -> 210.8 mm, vias 6 -> 7
- net RX: track 12.9 -> 56.4 mm
- net TX: track 12.6 -> 46.5 mm, vias 1 -> 0
- net VIN: track 67.2 -> 36.8 mm
- net DRB: track 1.53 -> 30.2 mm, vias 0 -> 2
- net SDB: track 1.53 -> 28.0 mm, vias 0 -> 2
- net Net-(D22-K): track 0.00 -> 22.1 mm
- net +5V: track 32.7 -> 54.7 mm
- net HOLA: track 1.80 -> 23.7 mm, vias 1 -> 2
- net HOLB: track 1.72 -> 20.9 mm, vias 1 -> 2
- net Net-(D3-K): track 31.1 -> 14.0 mm, vias 2 -> 0
- net HOLC: track 1.64 -> 17.1 mm, vias 1 -> 2
- net Net-(D1-K): track 4.75 -> 15.5 mm, vias 0 -> 2
- net Net-(D23-K): track 0.00 -> 10.6 mm
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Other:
- board outline added: 120.1 x 60.3 mm
